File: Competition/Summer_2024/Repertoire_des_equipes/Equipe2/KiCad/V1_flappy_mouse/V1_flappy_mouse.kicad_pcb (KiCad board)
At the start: 2 copper layers, 65 x 95 mm, 32 parts, among them J201 Conn_01x05_no_connect(SPI), J202 Conn_accelerometer_I2C, J203 Conn_Module_SD, J301 ESP_GAUCHE, J302 ESP_DROIT, J304 Conn_TFT_display, SW201 JS102011JAQN, U301 LM393

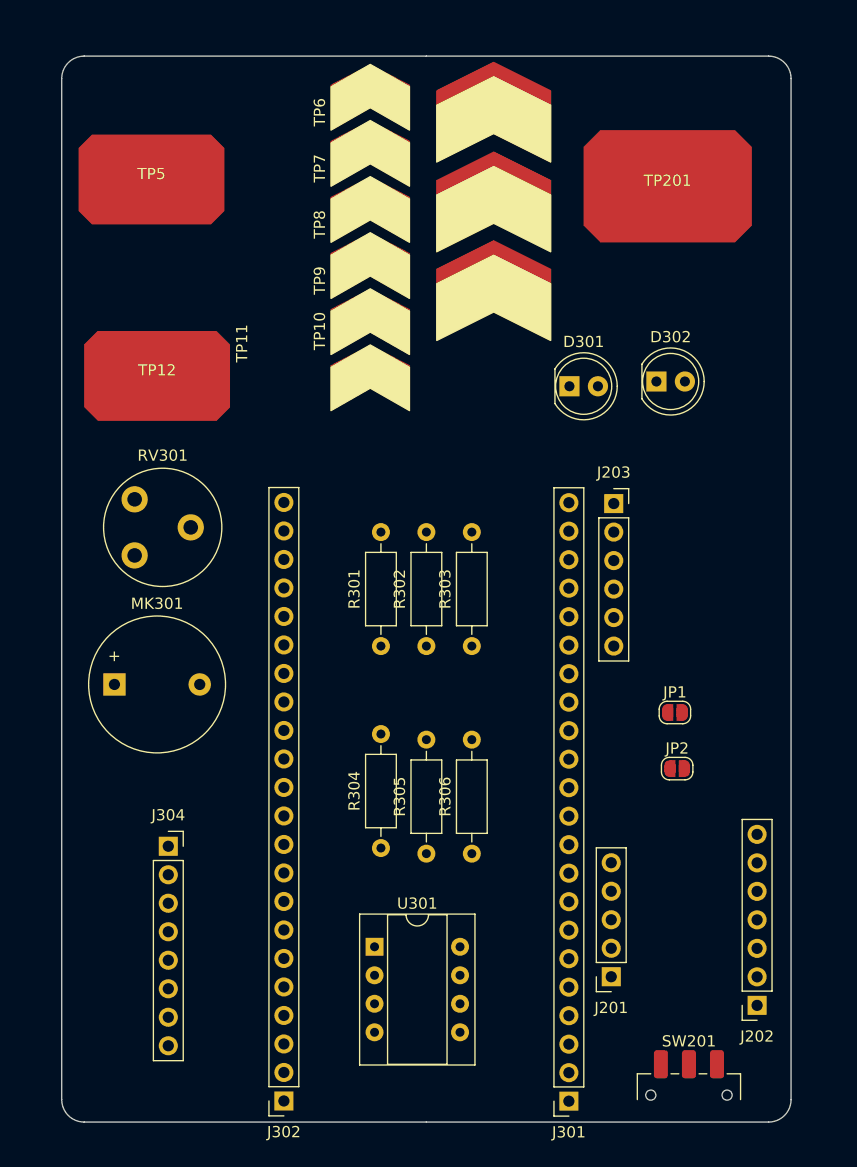
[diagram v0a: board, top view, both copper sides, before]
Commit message: Push de PCB compléter à 80%
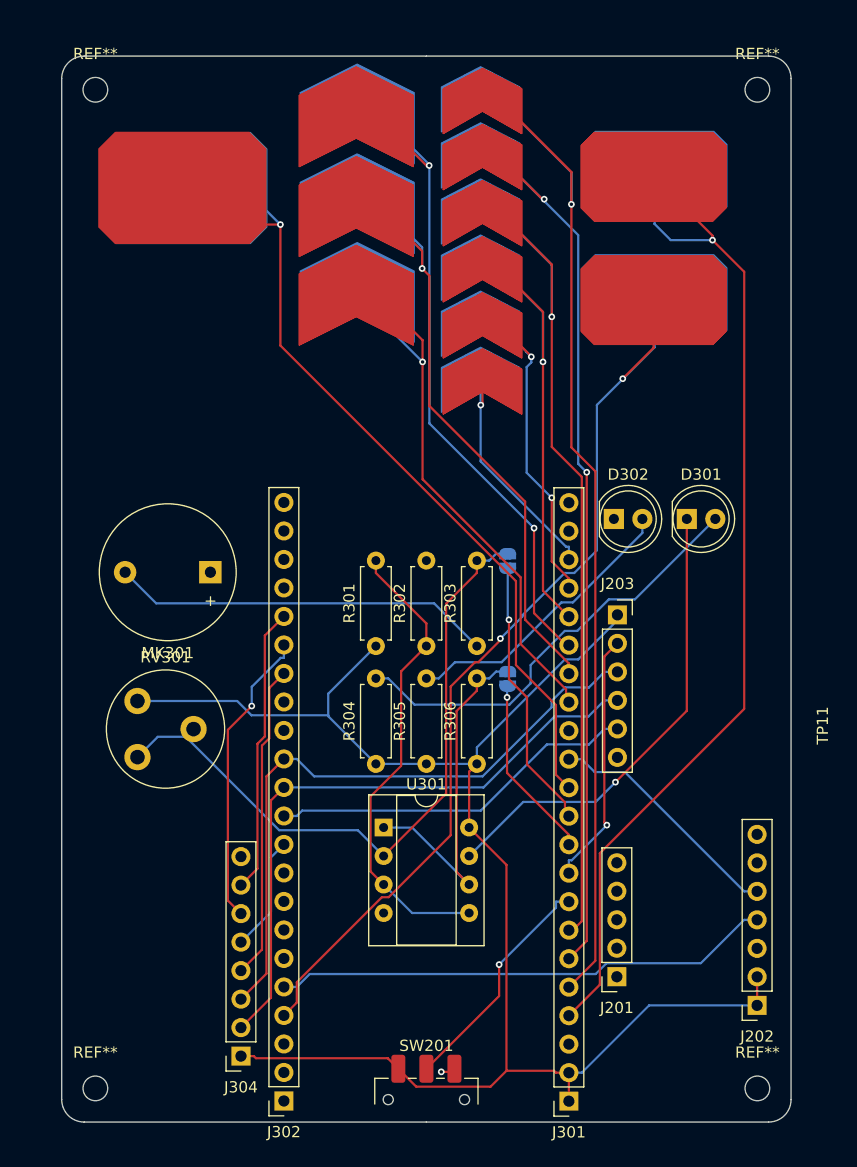
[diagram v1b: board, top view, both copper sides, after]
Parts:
- added ?: , , B.Cu at (126.2, 66.5)
- added ?: , , B.Cu at (137.5, 62.4)
- added ?: , , B.Cu at (152.8, 65.8)
- added ?: , , B.Cu at (152.8, 76.8)
- added ?: , , B.Cu at (110.8, 66.8)
- added ?: , , B.Cu at (137.5, 67.4)
- added ?: , , B.Cu at (126.2, 74.4)
- added ?: , , B.Cu at (137.5, 77.4)
- added ?: , , B.Cu at (126.2, 58.5)
- added ?: , , B.Cu at (137.5, 57.4)
- added ?: , , B.Cu at (137.5, 82.4)
- added ?: , , B.Cu at (137.5, 72.4)
- added REF**: MountingHole_2.2mm_M2, MountingHole:MountingHole_2.2mm_M2, F.Cu at (162.0, 147.0)
- added REF**: MountingHole_2.2mm_M2, MountingHole:MountingHole_2.2mm_M2, F.Cu at (103.0, 147.0)
- added REF**: MountingHole_2.2mm_M2, MountingHole:MountingHole_2.2mm_M2, F.Cu at (162.0, 58.0)
- added REF**: MountingHole_2.2mm_M2, MountingHole:MountingHole_2.2mm_M2, F.Cu at (103.0, 58.0)
- added TP10: Touchpad_scroll8, Librairie_touchpad:Touchpad_slider_smaller, F.Cu at (137.5, 75.9)
- added TP11: Touchpad_scroll9, Librairie_touchpad:Touchpad_slider_smaller, F.Cu at (137.5, 80.9)
- added TP12: Touchpad_stopMouseMotion, Librairie_touchpad:Touchpad_biz_rect_smaller, F.Cu at (152.8, 76.8)
- added TP202: Touchpad_scroll1, Librairie_touchpad:Touchpad_slider, F.Cu at (126.2, 74.4)
- added TP203: Touchpad_scroll2, Librairie_touchpad:Touchpad_slider, F.Cu at (126.2, 66.5)
- added TP204: Touchpad_scroll3, Librairie_touchpad:Touchpad_slider, F.Cu at (126.2, 58.5)
- added TP5: Touchpad_click_gauche, Librairie_touchpad:Touchpad_biz_rect_smaller, F.Cu at (152.8, 65.8)
- added TP6: Touchpad_scroll4, Librairie_touchpad:Touchpad_slider_smaller, F.Cu at (137.5, 55.9)
- added TP7: Touchpad_scroll5, Librairie_touchpad:Touchpad_slider_smaller, F.Cu at (137.5, 60.9)
- added TP8: Touchpad_scroll6, Librairie_touchpad:Touchpad_slider_smaller, F.Cu at (137.5, 65.9)
- added TP9: Touchpad_scroll7, Librairie_touchpad:Touchpad_slider_smaller, F.Cu at (137.5, 70.9)
- JP1, JP2, TP10, TP11, TP12, TP201, TP202, TP203, TP204, TP5, TP6, TP7, TP8, TP9: moved to B.Cu
- R301, R302, R303, R304, R305, R306: footprint Resistor_THT:R_Axial_DIN0207_L6.3mm_D2.5mm_P10.16mm_Horizontal -> Resistor_THT:R_Axial_DIN0207_L6.3mm_D2.5mm_P7.62mm_Horizontal
- moved TP12 44.9 mm to (152.8, 76.7), turned to 180 degrees
- moved TP5 44.8 mm to (152.8, 65.7), turned to 180 degrees
- moved TP201 43.2 mm to (110.8, 66.8), turned to 180 degrees
- moved SW201 23.4 mm to (132.5, 148.0)
- moved JP1 20.1 mm to (139.8, 100.0), turned to -90 degrees
- moved J304 19.8 mm to (116.0, 144.1), turned to 180 degrees
- moved RV301 18.0 mm to (106.8, 117.5)
- moved JP2 17.1 mm to (139.8, 110.5), turned to -90 degrees
- moved D301 15.8 mm to (155.7, 96.2)
- moved MK301 13.2 mm to (113.2, 101.0), turned to 180 degrees
- moved D302 12.8 mm to (149.2, 96.2)
- moved TP202 12.2 mm to (126.3, 74.2)
- moved TP203 12.2 mm to (126.3, 66.2)
- moved TP204 12.2 mm to (126.3, 58.2)
- moved U301 10.7 mm to (128.7, 123.8)
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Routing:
- net +3.3V: track 0.00 -> 144.1 mm
- net TOUCH5/GPIO5: track 0.00 -> 100.0 mm, vias 0 -> 1
- net TOUCH4/GPIO4: track 0.00 -> 94.7 mm, vias 0 -> 1
- net GPIO1/TOUCH1/ADC1_0/SDA0: track 0.00 -> 86.7 mm, vias 0 -> 2
- net TOUCH6/GPIO6: track 0.00 -> 85.6 mm, vias 0 -> 2
- net TOUCH7/GPIO7: track 0.00 -> 83.5 mm, vias 0 -> 1
- net TOUCH8/GPIO8: track 0.00 -> 80.9 mm, vias 0 -> 1
- net FSPID/TOUCH11/GPIO11: track 0.00 -> 66.3 mm, vias 0 -> 2
- net FSPICS0/TOUCH10/GPIO10: track 0.00 -> 61.5 mm, vias 0 -> 1
- net Net-(JP1-A): track 0.00 -> 60.8 mm
- net GPIO35/FSPID: track 0.00 -> 57.5 mm
- net FSPIHD/TOUCH9/GPIO9: track 0.00 -> 56.5 mm, vias 0 -> 1
- net GPIO36/FSPICLK: track 0.00 -> 55.9 mm
- net FSPICLK/TOUCH12/GPIO12: track 0.00 -> 48.0 mm, vias 0 -> 1
- net GPIO2/TOUCH2/ADC1_1/SCL1: track 0.00 -> 44.7 mm
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- added copper zone on In1.Cu, net GND
- added copper zone on In2.Cu, net GND
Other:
- copper layers 2 -> 4

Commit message: pcb 99% terminer
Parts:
- removed the ? at (126.2, 66.5)
- removed the ? at (137.5, 62.4)
- removed the ? at (137.5, 67.4)
- removed the ? at (126.2, 74.4)
- removed the ? at (137.5, 77.4)
- removed the ? at (126.2, 58.5)
- removed the ? at (137.5, 57.4)
- removed the ? at (137.5, 82.4)
- removed the ? at (137.5, 72.4)
- removed the TP10 at (137.5, 75.9)
- removed the TP10 at (137.3, 75.8)
- removed the TP11 at (137.5, 80.9)
- removed the TP11 at (137.3, 80.8)
- removed the TP6 at (137.5, 55.9)
- removed the TP6 at (137.3, 55.8)
- removed the TP7 at (137.5, 60.9)
- removed the TP7 at (137.3, 60.8)
- removed the TP8 at (137.5, 65.9)
- removed the TP8 at (137.3, 65.8)
- removed the TP9 at (137.5, 70.9)
- removed the TP9 at (137.3, 70.8)
- added TP10: Touchpad_scroll8, Librairie_touchpad:Touchpad_slider_smaller, F.Cu at (137.8, 63.5)
- added TP10: Touchpad_scroll8, Librairie_touchpad:Touchpad_slider_smaller, B.Cu at (136.8, 63.6)
- added TP11: Touchpad_scroll9, Librairie_touchpad:Touchpad_slider_smaller, F.Cu at (137.8, 58.5)
- added TP11: Touchpad_scroll9, Librairie_touchpad:Touchpad_slider_smaller, B.Cu at (136.8, 58.6)
- added TP6: Touchpad_scroll4, Librairie_touchpad:Touchpad_slider_smaller, F.Cu at (137.8, 83.5)
- added TP6: Touchpad_scroll4, Librairie_touchpad:Touchpad_slider_smaller, B.Cu at (136.8, 83.6)
- added TP7: Touchpad_scroll5, Librairie_touchpad:Touchpad_slider_smaller, F.Cu at (137.8, 78.5)
- added TP7: Touchpad_scroll5, Librairie_touchpad:Touchpad_slider_smaller, B.Cu at (136.8, 78.6)
- added TP8: Touchpad_scroll6, Librairie_touchpad:Touchpad_slider_smaller, F.Cu at (137.8, 73.5)
- added TP8: Touchpad_scroll6, Librairie_touchpad:Touchpad_slider_smaller, B.Cu at (136.8, 73.6)
- added TP9: Touchpad_scroll7, Librairie_touchpad:Touchpad_slider_smaller, F.Cu at (137.8, 68.5)
- added TP9: Touchpad_scroll7, Librairie_touchpad:Touchpad_slider_smaller, B.Cu at (136.8, 68.6)
- moved TP202 0.26 mm to (126.3, 74.2)
- moved TP203 0.26 mm to (126.3, 66.2)
- moved TP204 0.26 mm to (126.3, 58.2)
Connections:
- J304 pad 1: +3.3V -> GND
- J304 pad 2: GPIO36/FSPICLK -> +3.3V
- J304 pad 3: GPIO35/FSPID -> GPIO36/FSPICLK
- J304 pad 4: GPIO48/SPICLK_N -> GPIO35/FSPID
- J304 pad 5: GPIO38/FSPIWP/RGB_LED -> GPIO48/SPICLK_N
- J304 pad 6: GPIO47/SPICLK_P -> GPIO38/FSPIWP/RGB_LED
- J304 pad 7: GPIO21 -> GPIO47/SPICLK_P
- J304 pad 8: GND -> GPIO21
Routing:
- net TOUCH5/GPIO5: track 100.0 -> 61.2 mm, vias 1 -> 2
- net FSPIWP/TOUCH14/GPIO14: track 24.8 -> 48.6 mm
- net TOUCH6/GPIO6: track 85.6 -> 64.2 mm
- net TOUCH7/GPIO7: track 83.5 -> 67.3 mm, vias 1 -> 2
- net FSPIQ/TOUCH13/GPIO13: track 35.0 -> 45.7 mm
- net FSPIHD/TOUCH9/GPIO9: track 56.5 -> 46.8 mm
- net FSPICS0/TOUCH10/GPIO10: track 61.5 -> 51.9 mm
- net FSPID/TOUCH11/GPIO11: track 66.3 -> 57.5 mm
- net GPIO1/TOUCH1/ADC1_0/SDA0: track 86.7 -> 78.7 mm
- net FSPICLK/TOUCH12/GPIO12: track 48.0 -> 41.5 mm
- net TOUCH8/GPIO8: track 80.9 -> 74.6 mm
- net TOUCH4/GPIO4: track 94.7 -> 88.8 mm
- net GPIO36/FSPICLK: track 55.9 -> 53.4 mm
- net GPIO35/FSPID: track 57.5 -> 55.0 mm
- net GPIO38/FSPIWP/RGB_LED: track 10.3 -> 7.75 mm
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- added copper zone on B.Cu, net (none)
- added copper zone on F.Cu, net (none)
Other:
- board text added: "CLICK"
- board text added: "CLUNK"
- board text added: "PCB Flappy mouse V1 Par: Victor Larose & Jacob Turcotte Dans le contexte de CCI"
